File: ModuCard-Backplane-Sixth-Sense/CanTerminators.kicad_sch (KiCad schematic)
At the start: 20 parts, among them SW1 SW_DIP_x02, SW2 SW_DIP_x02, SW3 SW_DIP_x02, SW4 SW_DIP_x02

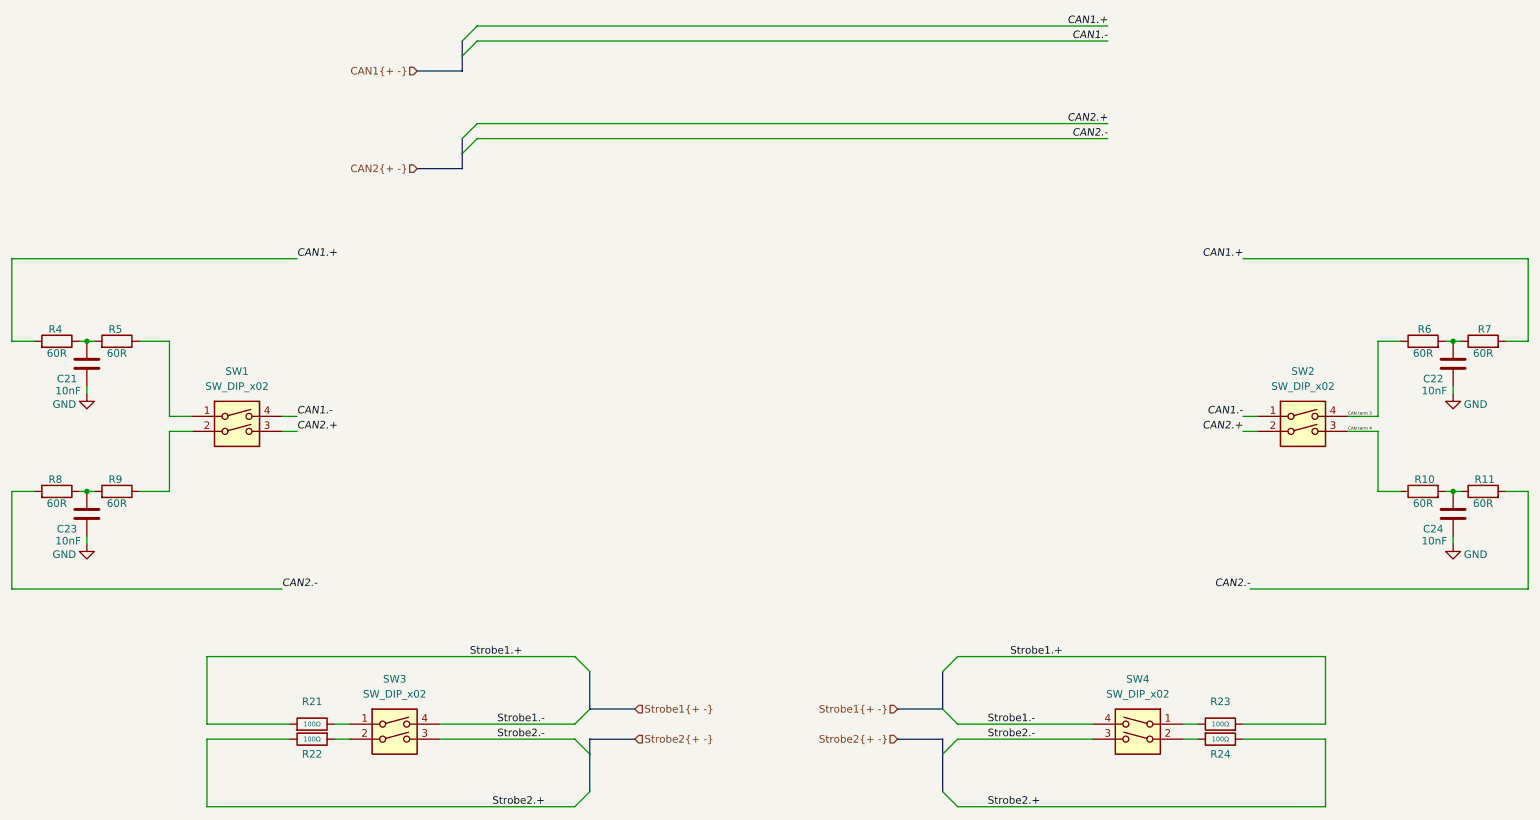
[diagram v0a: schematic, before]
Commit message: fix DRC errors, change pinout
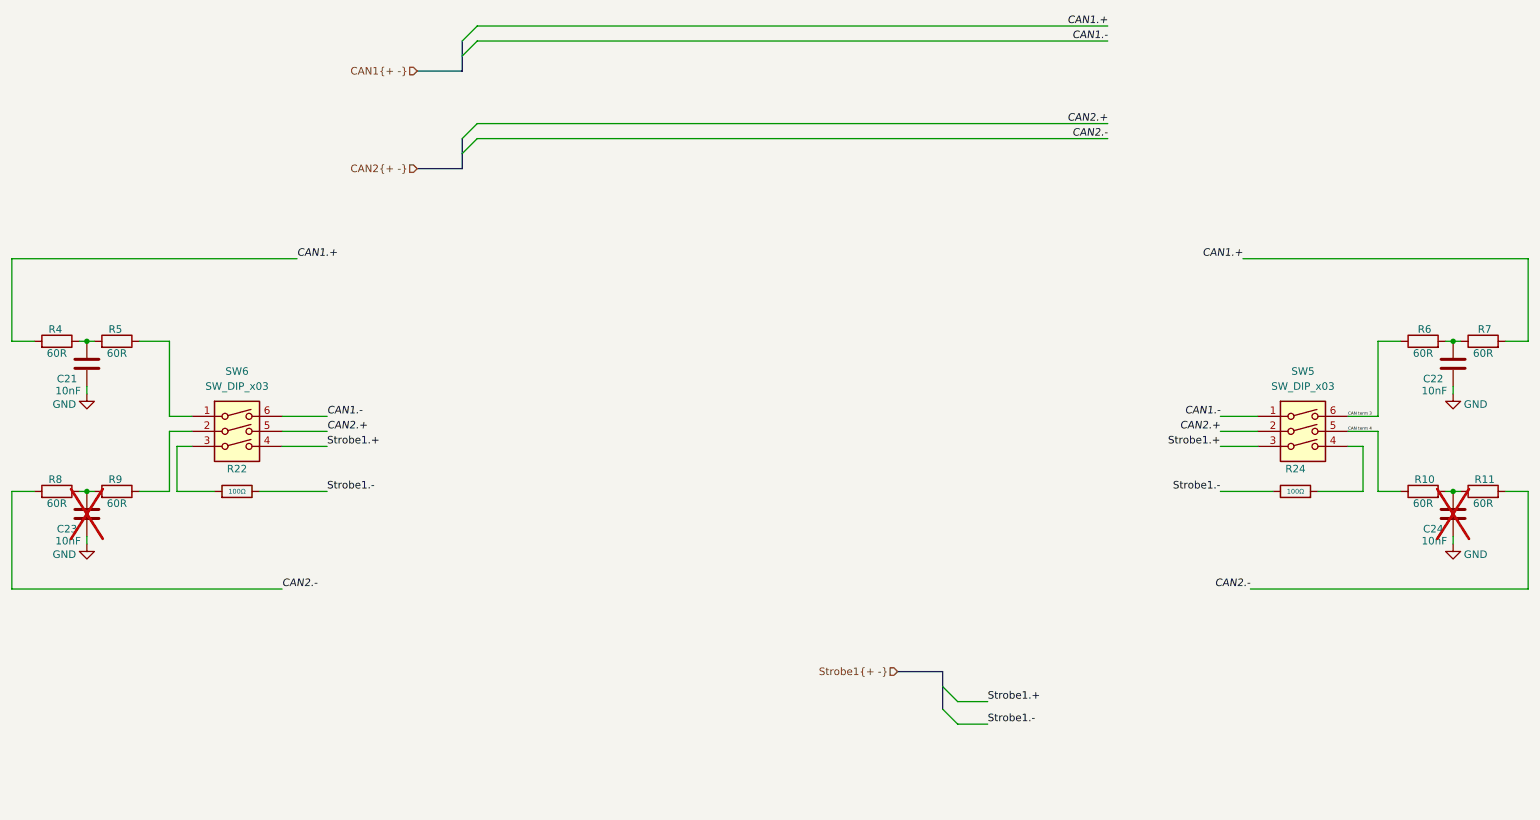
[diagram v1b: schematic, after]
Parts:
- removed R21, R23: 100Ω, PCM_JLCPCB:R_0603, symbol PCM_JLCPCB-Resistors:0603,100Ω
- removed SW1, SW2, SW3, SW4: SW_DIP_x02, Button_Switch_THT:SW_DIP_SPSTx02_Slide_9.78x7.26mm_W7.62mm_P2.54mm, symbol Switch:SW_DIP_x02
- added SW5, SW6: SW_DIP_x03, Button_Switch_THT:SW_DIP_SPSTx03_Slide_6.7x9.18mm_W7.62mm_P2.54mm_LowProfile, symbol Switch:SW_DIP_x03
- C23, C24: now not fitted; now left out of the parts list
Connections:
- net Strobe2.+ is gone; now on net Strobe1.-: R22.2, R24.2
- net CAN term 3: now also SW5.6
- net CAN term 4: now also SW5.5
- net CAN1.-: now also SW5.1, SW6.6
- net CAN2.+: now also SW5.2, SW6.5
- net Strobe1.+: now also SW5.3, SW6.4
- net at R24.1: now also SW5.4
- net at R22.1: now also SW6.3
- net at R5.1: now also SW6.1
- net at R9.1: now also SW6.2
